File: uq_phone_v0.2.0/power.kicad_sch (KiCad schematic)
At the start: 33 parts, among them J1 USB4105-GF-A, J2 BM03B-ACHSS-GAN-TF_LF__SN_, U1 MCP73871-2CCI_ML, U2 TPS62162DSGR, U3 BQ27441DRZR-G1A

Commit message: Clean repo
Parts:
- removed J1: USB4105-GF-A, USB_C_connector:GCT_USB4105-GF-A, symbol USB4105-GF-A:USB4105-GF-A
- removed R10: 0R, Resistor_SMD:R_0805_2012Metric, symbol Resistors:Resistor_0R_2A
- removed TP6: TestPoint, TestPoint:TestPoint_Pad_D1.5mm, symbol Connector:TestPoint
- added J2: 124018312112A, 124018312112A:AMPHENOL_124018312112A, symbol 124018312112A:124018312112A
- renumbered C4 to C1, C7 to C2, C1 to C3, C3 to C4, C2 to C7, J2 to J3, R11 to R1, R3 to R10, R4 to R11, R5 to R2, R6 to R3, R1 to R5, R9 to R6, R2 to R7, R7 to R8, R8 to R9, TP1 to TP2, TP5 to TP4, TP7 to TP5, TP2 to TP6, TP4 to TP7, U2 to U1, U1 to U2
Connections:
- net GND: now also J2.A1 (GND_A), J2.A12 (GND_A__1), J2.B1 (GND_B), J2.B12 (GND_B__1), J2.SH1 (SHIELD), J2.SH2 (SHIELD__1), J2.SH3 (SHIELD__2), J2.SH4 (SHIELD__3)
- net USB_N: now also J2.A7 (D1-), J2.B7 (D2-)
- net USB_P: now also J2.A6 (D1+), J2.B6 (D2+)
- net at R3.2: now also J2.B5 (CC2)
- net at R2.2: now also J2.A5 (CC1)
- new net: J2.A4 (VBUS_A), J2.A9 (VBUS_A__1)
- new net: J2.B4 (VBUS_B), J2.B9 (VBUS_B__1)
- no-connect marks 2 -> 10
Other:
- note removed: "Not sure about this, gapping to allow"
- moved on the sheet: B1, C3, C4, C7, J3, R10, R11, R2, R3, R5, R7, TP2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

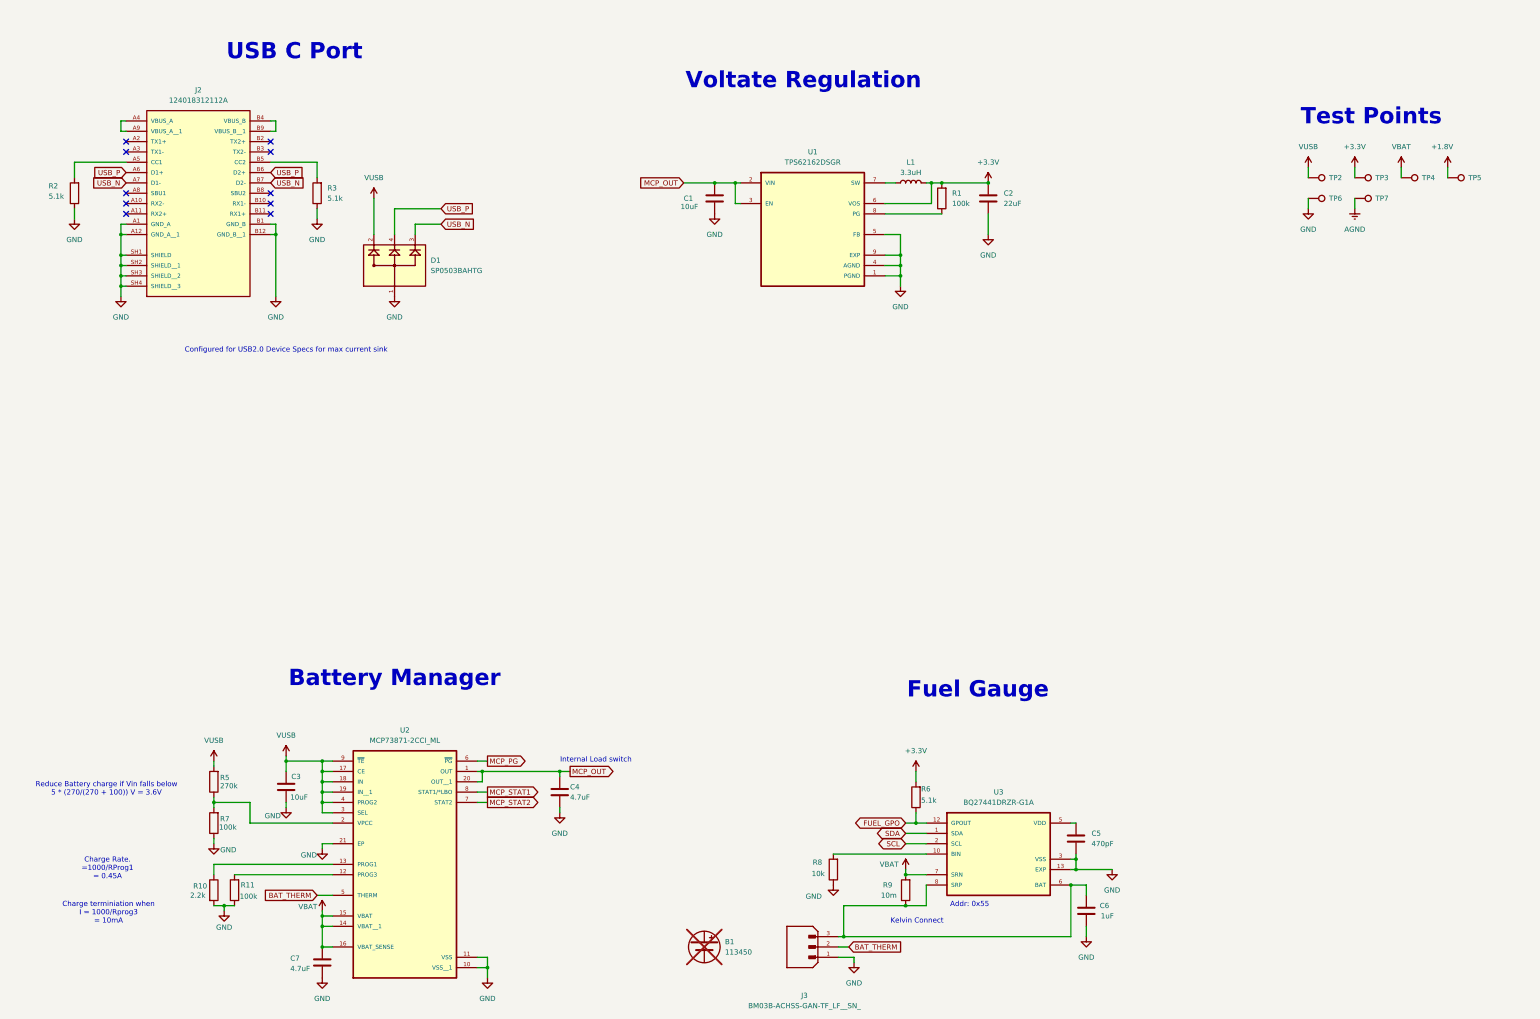
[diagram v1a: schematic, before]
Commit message: Add more footprints, reduce sizes
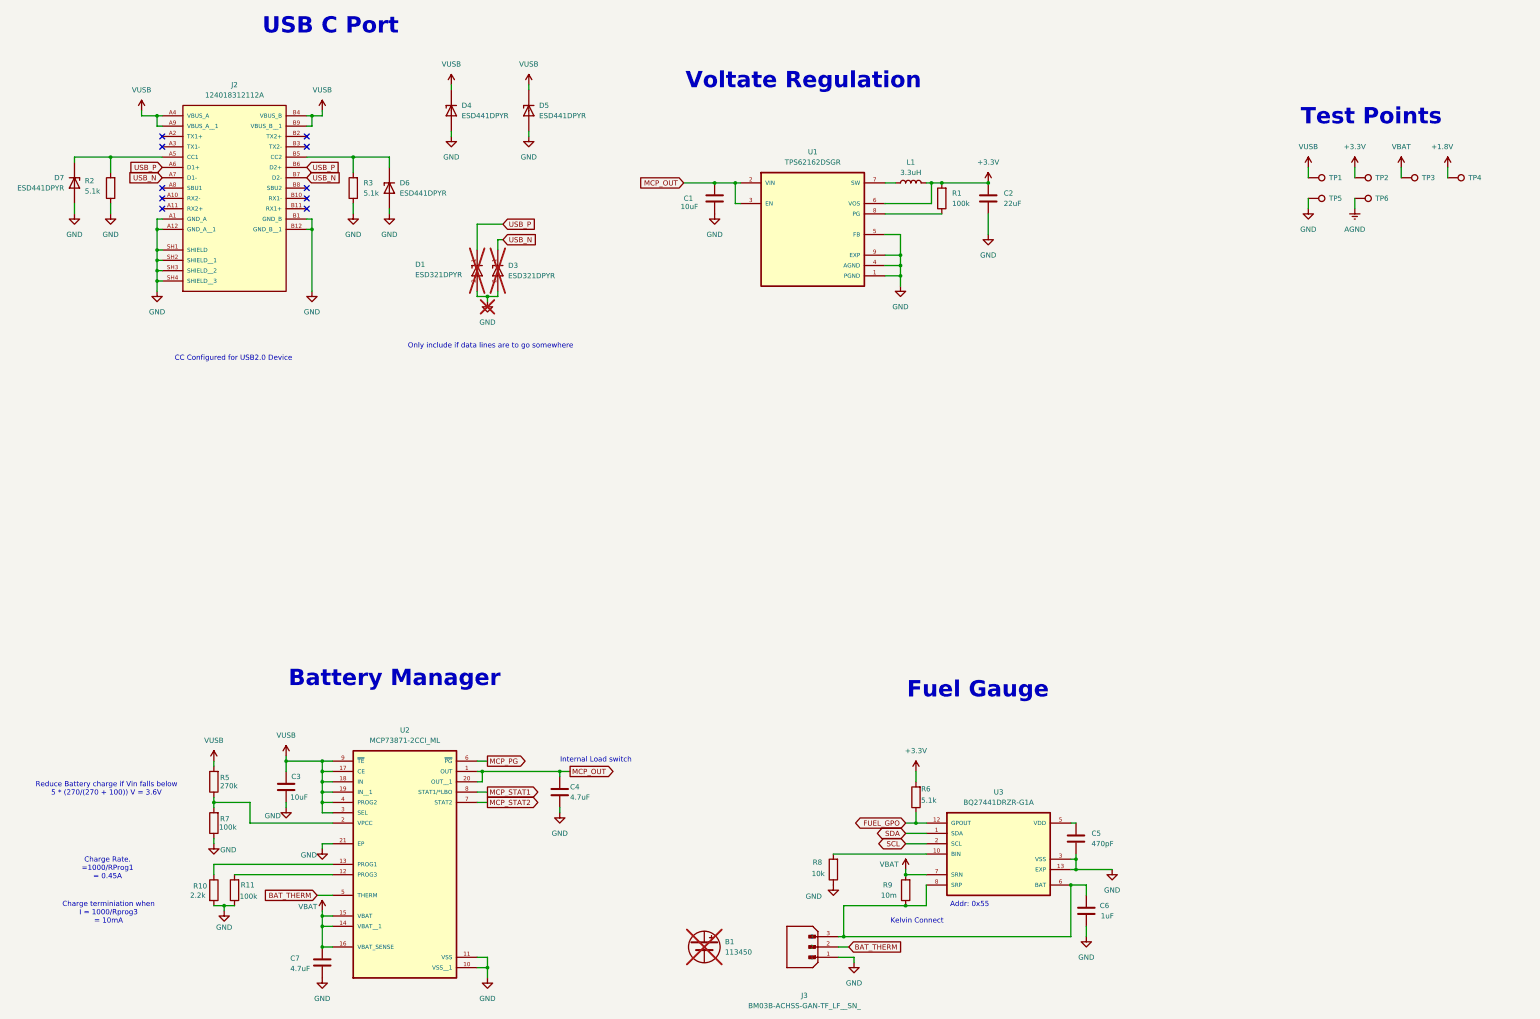
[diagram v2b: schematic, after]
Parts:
- removed D1: SP0503BAHTG, SP0503BAHTG:SOT143, symbol SP0503BAHTG:SP0503BAHTG
- removed TP7: TestPoint, TestPoint:TestPoint_Pad_D1.5mm, symbol Connector:TestPoint
- added D1, D3: ESD321DPYR, ESD321DPYR:TVS_ESD321DPYR, symbol ESD321DPYR:ESD321DPYR
- added D4, D5, D6, D7: ESD441DPYR, ESD441DPLR:DIODFN60X30X32-2N, symbol ESD441DPYR:ESD441DPYR
- added TP1: TestPoint, TestPoint:TestPoint_Pad_D1.5mm, symbol Connector:TestPoint
- C4, C7: footprint Capacitor_SMD:C_0402_1005Metric -> Capacitor_SMD:C_0201_0603Metric; LCSC PN C191541 -> C335103
- C6: footprint Capacitor_SMD:C_0402_1005Metric -> Capacitor_SMD:C_0201_0603Metric; LCSC PN C52923 -> C53067
- R1, R11, R7: footprint Resistor_SMD:R_0402_1005Metric -> Resistor_SMD:R_0201_0603Metric; LCSC PN C606167 -> C106224
- R10: footprint Resistor_SMD:R_0402_1005Metric -> Resistor_SMD:R_0201_0603Metric; LCSC PN C606171 -> C142018
- R2, R3, R6: footprint Resistor_SMD:R_0402_1005Metric -> Resistor_SMD:R_0201_0603Metric; LCSC PN C7334585 -> C274341
- R8: footprint Resistor_SMD:R_0402_1005Metric -> Resistor_SMD:R_0201_0603Metric; LCSC PN C851848 -> C106225
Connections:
- net +1.8V: now also TP4.1; no longer TP5.1
- net +3.3V: now also TP2.1; no longer TP3.1
- net AGND: now also TP6.1
- net GND: now also TP5.1, D1.2, D3.2, D4.2, D5.2, D6.2, D7.2; no longer TP6.1
- net USB_N: now also D3.1
- net USB_P: now also D1.1
- net VBAT: now also TP3.1; no longer TP4.1
- net VUSB: now also J2.A4 (VBUS_A), J2.A9 (VBUS_A__1), J2.B4 (VBUS_B), J2.B9 (VBUS_B__1), D4.1, D5.1, TP1.1; no longer TP2.1
- net at J2.A5 (CC1), R2.2: now also D7.1
- net at J2.B5 (CC2), R3.2: now also D6.1
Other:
- note added: "CC Configured for USB2.0 Device"
- note added: "Only include if data lines are to go somewhere"
- note removed: "Configured for USB2.0 Device Specs for max current sink"
- moved on the sheet: J2, R2, R3

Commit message: Various Changes to footprints and components
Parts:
- added C30: 1uF, Capacitor_SMD:C_0201_0603Metric, symbol Capacitors:Capacitor_1uF
- added C31: 100nF, Capacitor_SMD:C_0201_0603Metric, symbol Capacitors:capacitor_100nF
- added TP7: TestPoint, TestPoint:TestPoint_Pad_D1.5mm, symbol Connector:TestPoint
- added U15: TPS22964CYZPR, TPS22964CYZPR:IC_SN74LVC2G34YZPR, symbol TPS22964CYZPR:TPS22964CYZPR
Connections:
- net +3.3V: now also C30.1, U15.A2 (VIN), U15.B2 (VIN)
- net AGND: now also TP7.1; no longer TP6.1
- net GND: now also TP6.1, C30.2, C31.2, U15.C1 (GND); no longer TP5.1
- new net +3.3V_SW: C31.1, TP5.1, U15.A1 (VOUT), U15.B1 (VOUT)
- new net POWER_SW: U15.C2 (ON)
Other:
- note added: "Load Switch"
- title: Power System -> UQ Phone
- moved on the sheet: B1, C1, C2, C3, C4, C5, C6, C7, J3, L1, R1, R10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

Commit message: Minor Changes - new display
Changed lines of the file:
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@@
 	(text "CC Configured for USB2.0 Device"
 		(exclude_from_sim no)
-		(at 68.326 102.87 0)
+		(at 68.072 99.06 0)
 		(effects
 			(font
@@
 	(wire
 		(pts
-			(xy 121.92 48.26) (xy 121.92 46.99)
-		)
-		(stroke
-			(width 0)
-			(type default)
-		)
-	)
-	(wire
-		(pts
 			(xy 49.53 83.82) (xy 50.8 83.82)
 		)
@@
 		)
 		(stroke
+			(width 0)
+			(type default)
+		)
+	)
+	(wire
+		(pts
+			(xy 121.92 46.99) (xy 121.92 48.26)
+		)
+		(stroke

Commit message: New HP jack, move stuff out for new arrangement
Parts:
- removed R6: 5.1k, Resistor_SMD:R_0201_0603Metric, symbol Resistors:Resistor_5k1
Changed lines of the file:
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@@
 	)
 	(junction
-		(at 233.68 181.61)
-		(diameter 0)
-		(color 0 0 0 0)
-	)
-	(junction
 		(at 273.05 193.04)
 		(diameter 0)
@@
 	(wire
 		(pts
-			(xy 236.22 181.61) (xy 233.68 181.61)
+			(xy 231.14 181.61) (xy 236.22 181.61)
 		)
 		(stroke
@@
 	(wire
 		(pts
-			(xy 233.68 181.61) (xy 233.68 179.07)
-		)
-		(stroke
-			(width 0)
-			(type default)
-		)
-	)
-	(wire
-		(pts
 			(xy 72.39 176.53) (xy 72.39 177.8)
 		)
@@
 	(wire
 		(pts
-			(xy 233.68 168.91) (xy 233.68 171.45)
-		)
-		(stroke
-			(width 0)
-			(type default)
-		)
-	)
-	(wire
-		(pts
 			(xy 266.7 60.96) (xy 266.7 55.88)
 		)
@@
 	(wire
 		(pts
-			(xy 231.14 181.61) (xy 233.68 181.61)
-		)
-		(stroke
-			(width 0)
-			(type default)
-		)
-	)
-	(wire
-		(pts
 			(xy 330.2 172.72) (xy 346.71 172.72)
 		)
@@
 	)
 	(symbol
-		(lib_id "power:+3.3V")
-		(at 233.68 168.91 0)
-		(unit 1)
-		(exclude_from_sim no)
-		(in_bom yes)
-		(on_board yes)
-		(dnp no)
-		(fields_autoplaced yes)
-		(property "Reference" "#PWR022"
-			(at 233.68 172.72 0)
-			(effects
-				(font
-					(size 1.27 1.27)
-				)
-				(hide yes)
-			)
-		)
-		(property "Value" "+3.3V"
-			(at 233.68 163.83 0)
-			(effects
-				(font
-					(size 1.27 1.27)
-				)
-			)
-		)
-		(property "Footprint" ""
-			(at 233.68 168.91 0)
-			(effects
-				(font
-					(size 1.27 1.27)
-				)
-				(hide yes)
-			)
-		)
-		(property "Datasheet" ""
-			(at 233.68 168.91 0)
-			(effects
-				(font
-					(size 1.27 1.27)
-				)
-				(hide yes)
-			)
-		)
-		(property "Description" "Power symbol creates a global label with name \"+3.3V\""
-			(at 233.68 168.91 0)
-			(effects
-				(font
-					(size 1.27 1.27)
-				)
-				(hide yes)
-			)
-		)
-		(pin "1"
-		)
-		(instances
-			(project "uq_phone"
-				(path "/14f57415-6807-40a5-bb38-3cb818a2cdae/e697a7f0-03cd-4a38-a369-080a37468a6a"
-					(reference "#PWR022")
-					(unit 1)
-				)
-			)
-		)
-	)
-	(symbol
 		(lib_id "power:GND")
 		(at 275.59 209.55 0)
@@
 					(unit 1)
 				)
-			)
-		)
-	)
-	(symbol
-		(lib_id "Resistors:Resistor_5k1")
-		(at 233.68 175.26 0)
-		(unit 1)
-		(exclude_from_sim no)
-		(in_bom yes)
-		(on_board yes)
-		(dnp no)
-		(property "Reference" "R6"
-			(at 234.95 173.228 0)
-			(effects
-				(font
-					(size 1.27 1.27)
-				)
-				(justify left)
-			)
-		)
-		(property "Value" "5.1k"
-			(at 234.95 176.022 0)
-			(effects
-				(font
-					(size 1.27 1.27)
-				)
-				(justify left)
-			)
-		)
-		(property "Footprint" "Resistor_SMD:R_0201_0603Metric"
-			(at 233.68 179.07 0)
-			(effects
-				(font
-					(size 1.27 1.27)
-				)
-				(hide yes)
-			)
-		)
-		(property "Datasheet" ""
-			(at 233.68 179.07 0)
-			(effects
-				(font
-					(size 1.27 1.27)
-				)
-				(hide yes)
-			)
-		)
-		(property "Description" "50mW Thick Film Resistor 25V ±1% ±200ppm/℃ 5.1kΩ 0201 Chip Resistor - Surface Mount ROHS"
-			(at 233.68 179.07 0)
-			(effects
-				(font
-					(size 1.27 1.27)
-				)
-				(hide yes)
-			)
-		)
-		(property "LCSC PN" "C274341"
-			(at 233.68 175.26 0)
-			(effects
-				(font
-					(size 1.27 1.27)
-				)
-				(hide yes)
-			)
-		)
-		(pin "2"
-		)
-		(pin "1"
-		)
-		(instances
-			(project "uq_phone"
-				(path "/14f57415-6807-40a5-bb38-3cb818a2cdae/e697a7f0-03cd-4a38-a369-080a37468a6a"
-					(reference "R6")
-					(unit 1)
-				)

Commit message: New Layout
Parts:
- R5: footprint Resistor_SMD:R_0402_1005Metric -> Resistor_SMD:R_0201_0603Metric; LCSC PN C131553 -> C851694
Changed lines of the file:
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@@
 			)
 		)
-		(property "Footprint" "Resistor_SMD:R_0402_1005Metric"
+		(property "Footprint" "Resistor_SMD:R_0201_0603Metric"
 			(at 72.39 176.53 0)
 			(effects
@@
 			)
 		)
-		(property "Description" "RES SMD 270K OHM 1% 1/10W 0402"
+		(property "Description" "50mW Thick Film Resistor 25V ±200ppm/℃ ±0.5% 270kΩ 0201 Chip Resistor - Surface Mount ROHS"
 			(at 72.39 176.53 0)
 			(effects
@@
 			)
 		)
-		(property "LCSC PN" "C131553"
+		(property "LCSC PN" "C851694"
 			(at 72.39 172.72 0)
 			(effects

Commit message: DRC and routing fixing
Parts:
- removed TP4, TP7: TestPoint, TestPoint:TestPoint_Pad_D1.5mm, symbol Connector:TestPoint
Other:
- moved on the sheet: TP5

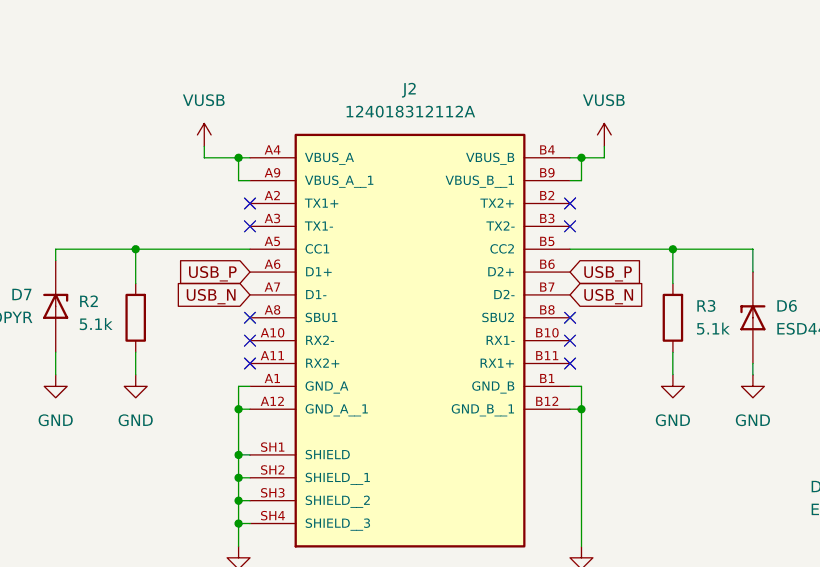
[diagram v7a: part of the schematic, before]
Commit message: New HP jack and circuit
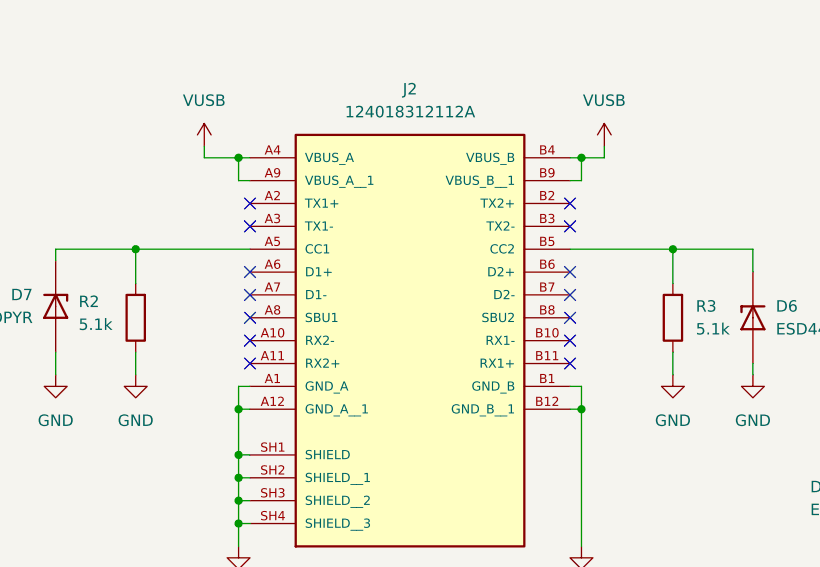
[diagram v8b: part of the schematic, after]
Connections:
- net USB_N: no longer J2.A7 (D1-), J2.B7 (D2-)
- net USB_P: no longer J2.A6 (D1+), J2.B6 (D2+)
- no-connect marks 10 -> 14
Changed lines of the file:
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@@
+	)
+	(no_connect
+		(at 50.8 58.42)
+	)
+	(no_connect
+		(at 86.36 58.42)
 	)
 	(no_connect
@@
 	(no_connect
 		(at 86.36 48.26)
+	)
+	(no_connect
+		(at 50.8 55.88)
+	)
+	(no_connect
+		(at 86.36 55.88)
 	)
 	(no_connect
@@
 		)
 	)
-	(global_label "USB_P"
-		(shape input)
-		(at 50.8 55.88 180)
-		(fields_autoplaced yes)
-		(effects
-			(font
-				(size 1.27 1.27)
-			)
-			(justify right)
-		)
-		(property "Intersheetrefs" "${INTERSHEET_REFS}"
-			(at 41.7672 55.88 0)
-			(effects
-				(font
-					(size 1.27 1.27)
-				)
-				(justify right)
-				(hide yes)
-			)
-		)
-	)
 	(global_label "FUEL_GPO"
 		(shape bidirectional)
@@
 		)
 	)
-	(global_label "USB_P"
-		(shape input)
-		(at 86.36 55.88 0)
-		(fields_autoplaced yes)
-		(effects
-			(font
-				(size 1.27 1.27)
-			)
-			(justify left)
-		)
-		(property "Intersheetrefs" "${INTERSHEET_REFS}"
-			(at 95.3928 55.88 0)
-			(effects
-				(font
-					(size 1.27 1.27)
-				)
-				(justify left)
-				(hide yes)
-			)
-		)
-	)
 	(global_label "MCP_STAT1"
 		(shape output)
@@
 		)
 	)
-	(global_label "USB_N"
-		(shape input)
-		(at 86.36 58.42 0)
-		(fields_autoplaced yes)
-		(effects
-			(font
-				(size 1.27 1.27)
-			)
-			(justify left)
-		)
-		(property "Intersheetrefs" "${INTERSHEET_REFS}"
-			(at 95.4533 58.42 0)
-			(effects
-				(font
-					(size 1.27 1.27)
-				)
-				(justify left)
-				(hide yes)
-			)
-		)
-	)
 	(global_label "BAT_THERM"
 		(shape input)
@@
 				(hide yes)
 			)
-		)
-	)
-	(global_label "USB_N"
-		(shape input)
-		(at 50.8 58.42 180)
-		(fields_autoplaced yes)
-		(effects
-			(font
-				(size 1.27 1.27)
-			)
-			(justify right)
-		)
-		(property "Intersheetrefs" "${INTERSHEET_REFS}"
-			(at 41.7067 58.42 0)
-			(effects
-				(font
-					(size 1.27 1.27)
-				)
-				(justify right)
-				(hide yes)
-			)
